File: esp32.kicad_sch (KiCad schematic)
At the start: 15 parts, among them IC3 ESP32-C3-WROOM-02-N4, J5 UART, J6 ToSSR, Q1 BSS138, SW1 SW_Push

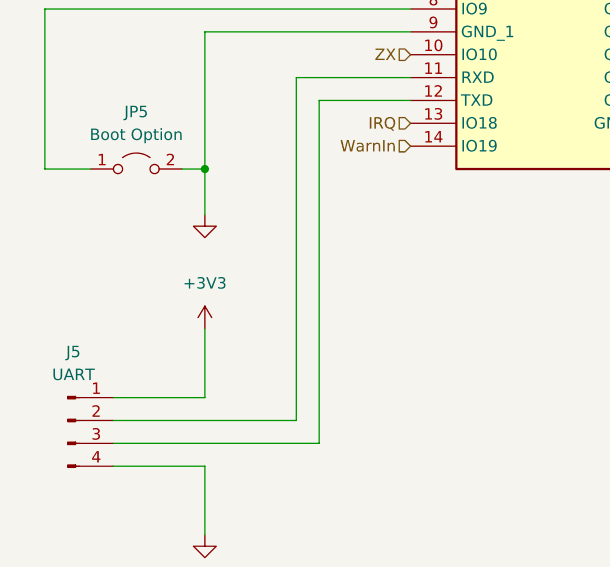
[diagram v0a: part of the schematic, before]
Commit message: feat: add +5V power symbol for uart programming
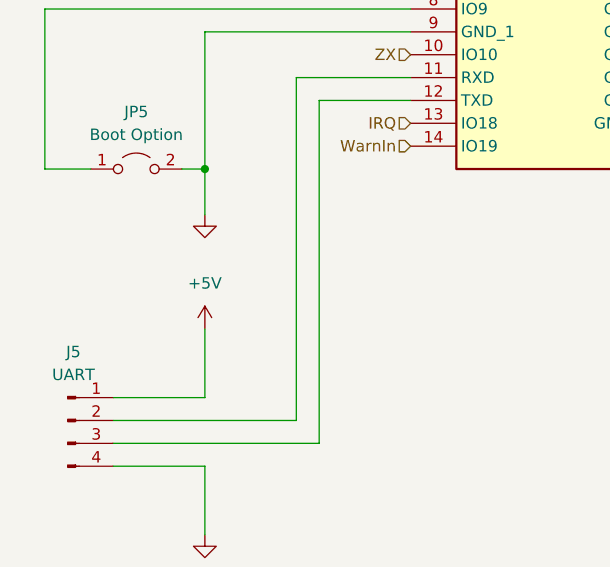
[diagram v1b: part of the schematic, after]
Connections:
- net +3V3: no longer J5.1 (Pin_1)
- new net +5V: J5.1 (Pin_1)

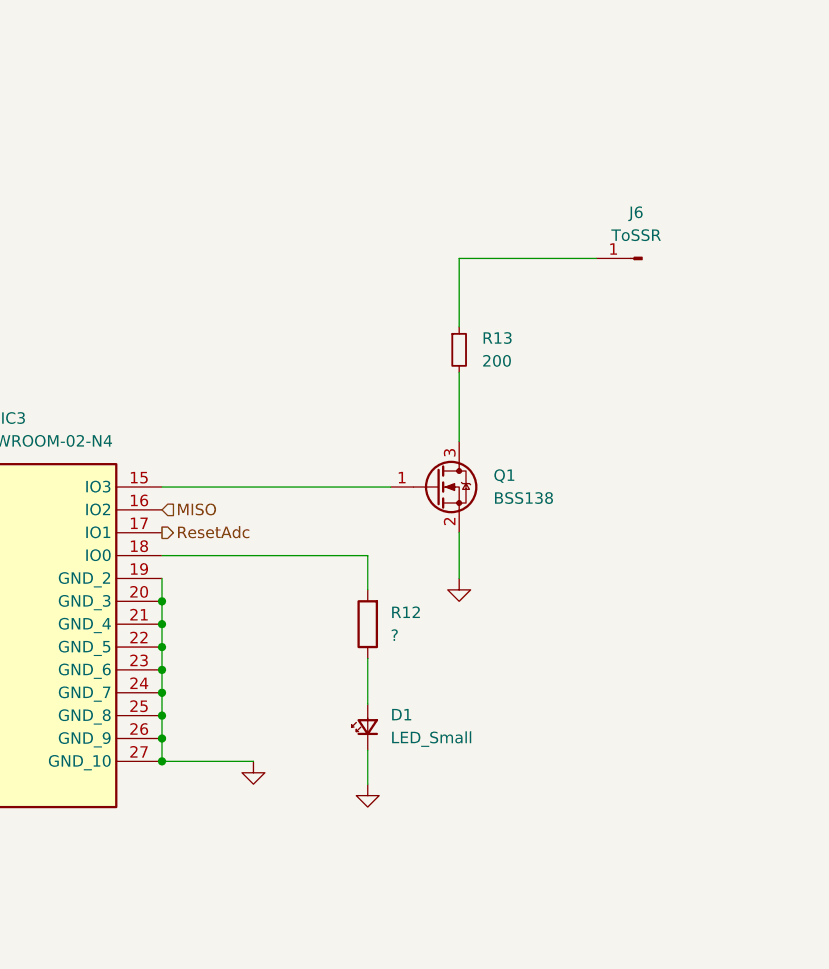
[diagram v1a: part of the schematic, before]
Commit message: fix: update esp32 strapping pad 2 to high level
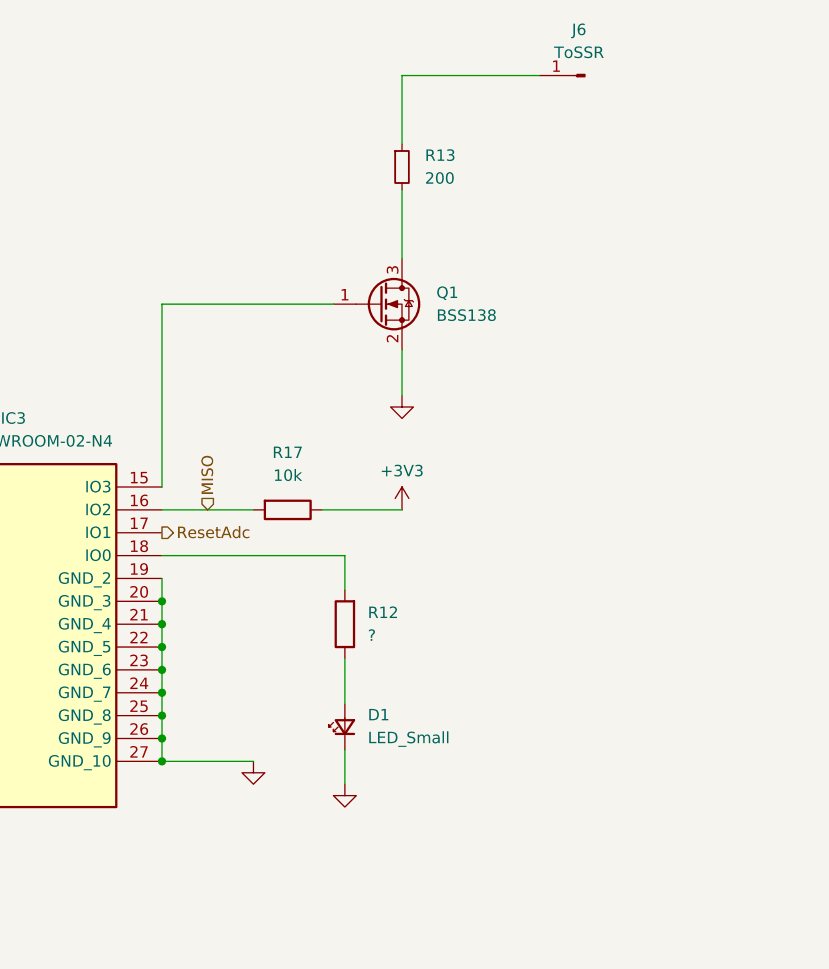
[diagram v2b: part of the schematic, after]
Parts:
- added R17: 10k, Resistor_THT:R_Axial_DIN0207_L6.3mm_D2.5mm_P7.62mm_Horizontal, symbol Device:R
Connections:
- net +3V3: now also R17.1
- net MISO: now also R17.2
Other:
- moved on the sheet: D1, J6, Q1, R12, R13

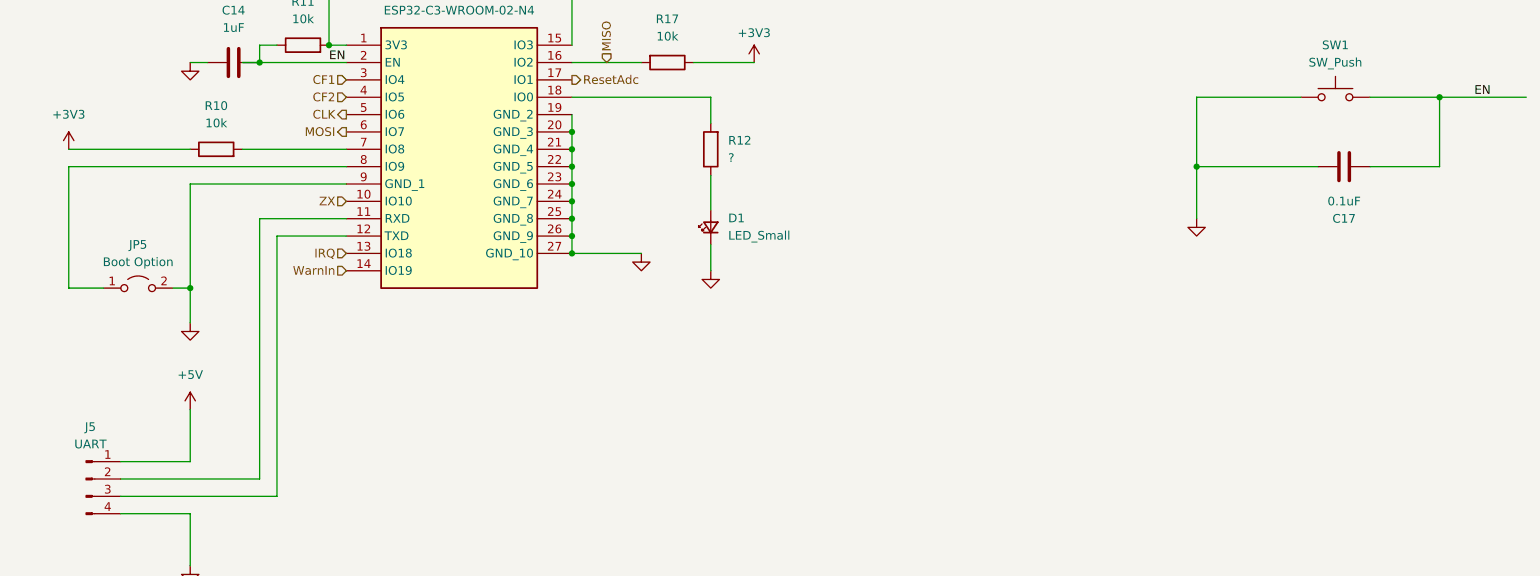
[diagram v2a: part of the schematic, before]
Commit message: fix: add boot button for esp32
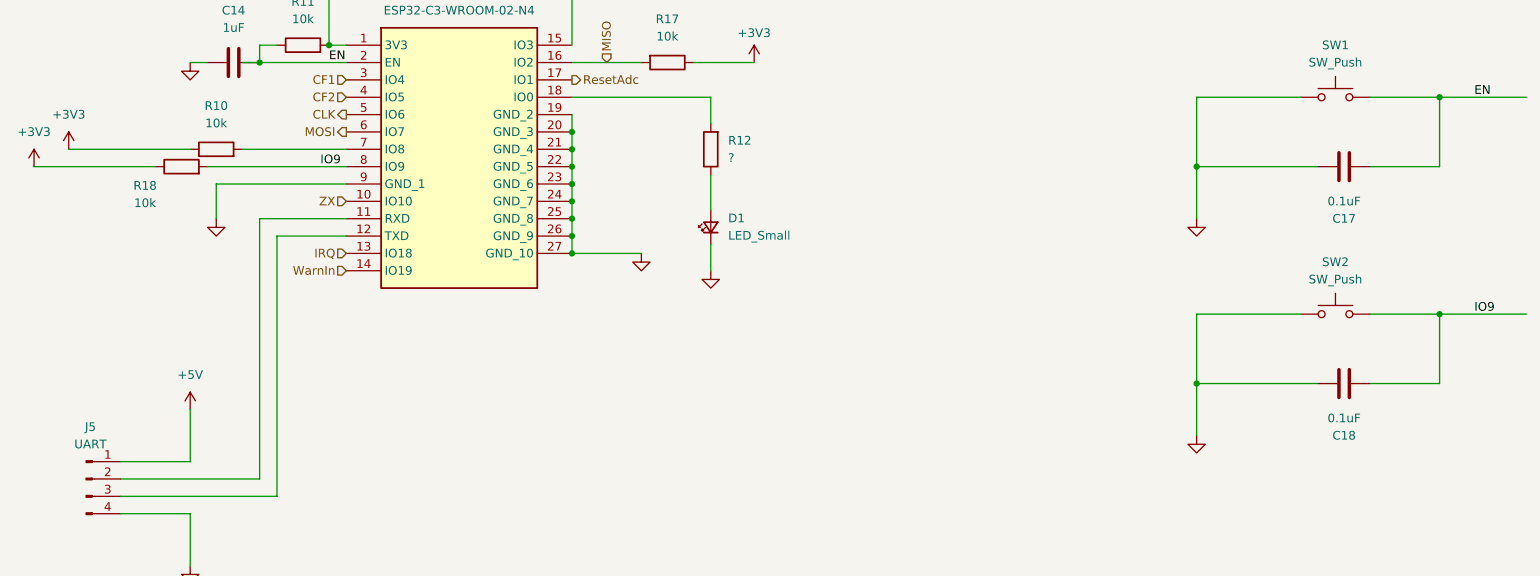
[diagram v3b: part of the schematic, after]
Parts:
- removed JP5: Boot Option, TestPoint:TestPoint_2Pads_Pitch2.54mm_Drill0.8mm, symbol Jumper:Jumper_2_Open
- added C18: 0.1uF, Capacitor_SMD:C_0805_2012Metric_Pad1.18x1.45mm_HandSolder, symbol Device:C
- added R18: 10k, Resistor_THT:R_Axial_DIN0207_L6.3mm_D2.5mm_P7.62mm_Horizontal, symbol Device:R
- added SW2: SW_Push, Button_Switch_SMD:SW_SPST_EVQQ2, symbol Switch:SW_Push
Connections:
- net +3V3: now also R18.1
- net GND: now also C18.1, SW2.1
- net IO9: now reaches IC3.8 (IO9)
- net IO9: now also C18.2, R18.2, SW2.2

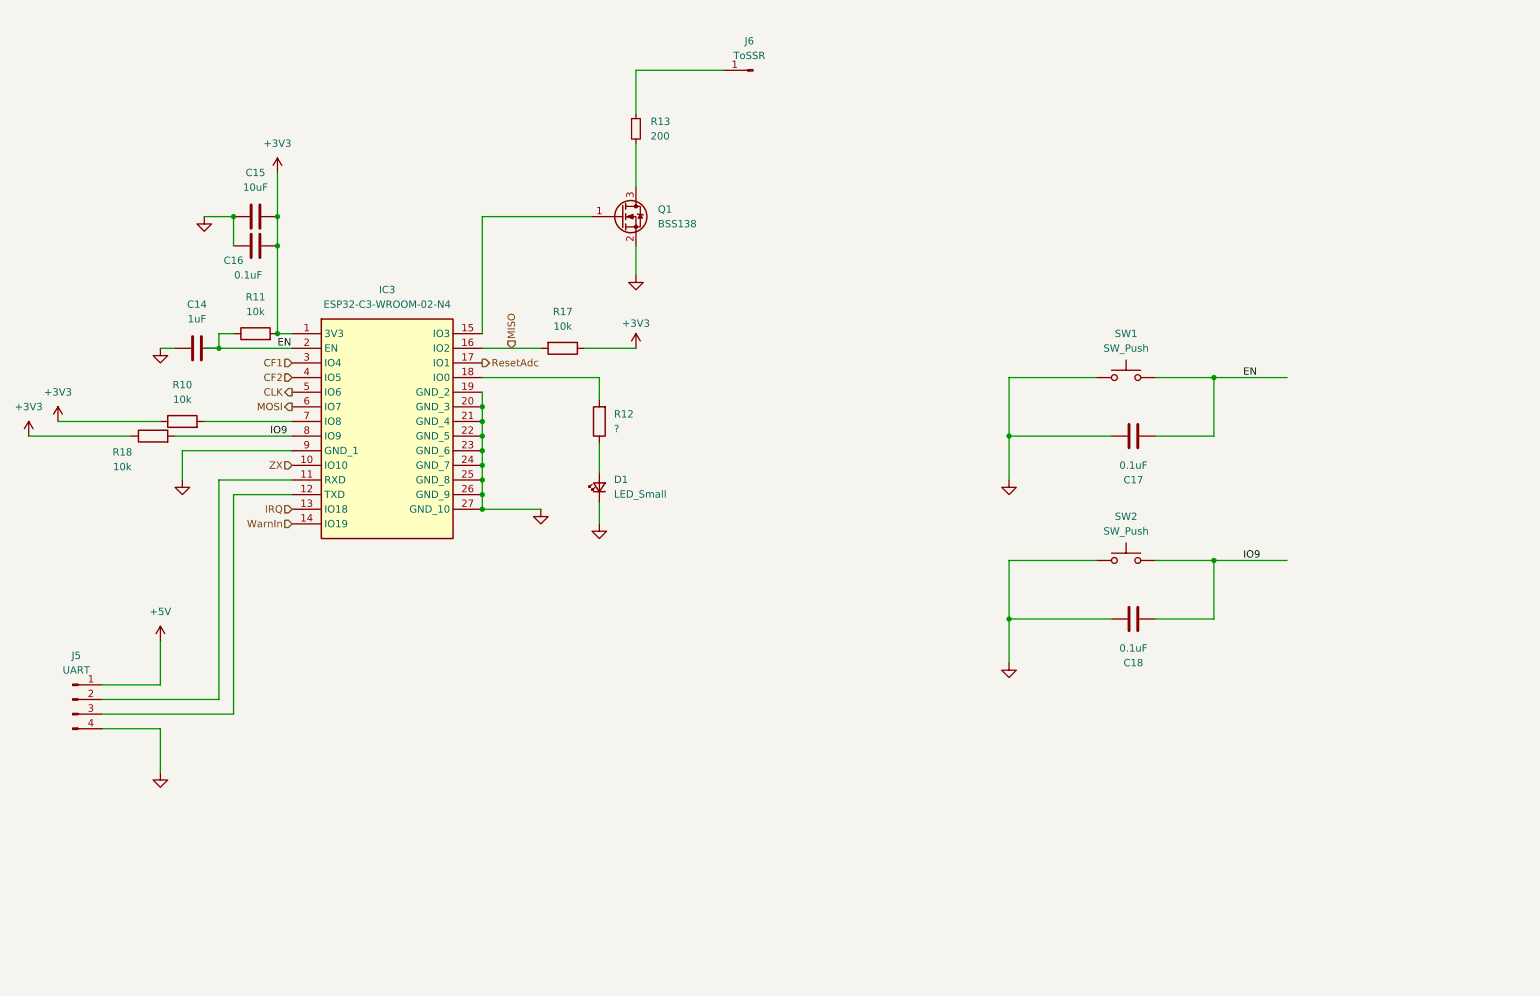
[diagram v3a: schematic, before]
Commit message: feat: substitute esp32-c3 with esp32-s3
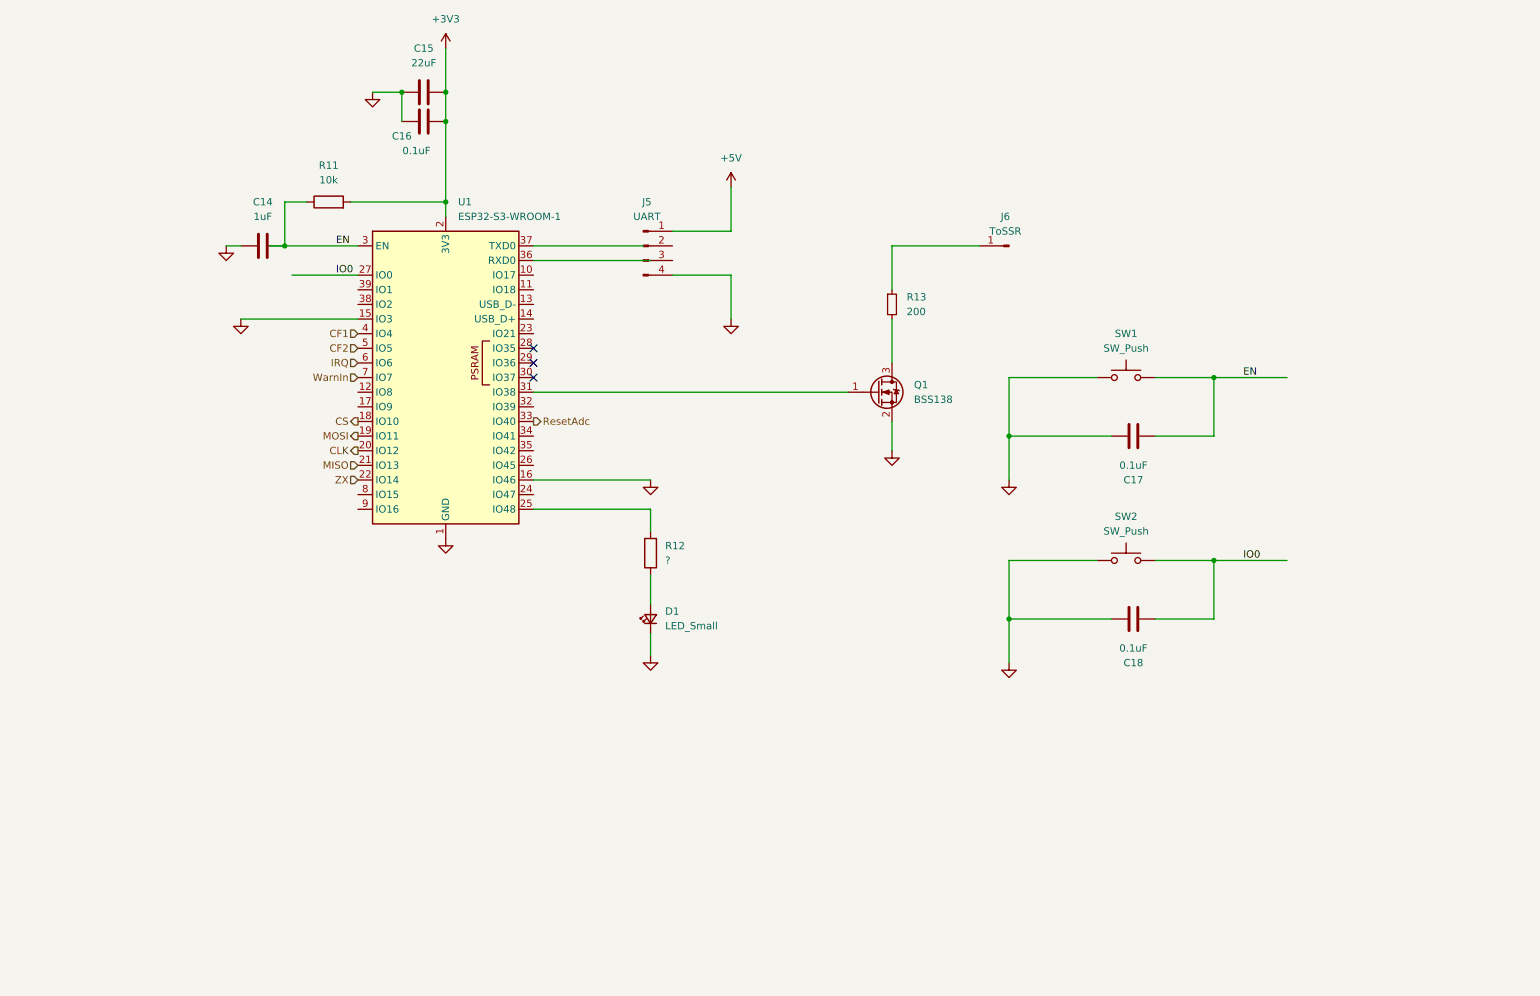
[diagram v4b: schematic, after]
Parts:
- removed IC3: ESP32-C3-WROOM-02-N4, ESP32-C3-WROOM-02-N4:ESP32C3WROOM02N4, symbol ESP32-C3-WROOM-02-N4:ESP32-C3-WROOM-02-N4
- removed R10, R17, R18: 10k, Resistor_THT:R_Axial_DIN0207_L6.3mm_D2.5mm_P7.62mm_Horizontal, symbol Device:R
- added U1: ESP32-S3-WROOM-1, RF_Module:ESP32-S3-WROOM-1, symbol RF_Module:ESP32-S3-WROOM-1
- C15: value 10uF -> 22uF
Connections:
- net +3V3: now also U1.2 (3V3)
- net CF1: now also U1.4 (IO4)
- net CF2: now also U1.5 (IO5)
- net CLK: now also U1.20 (IO12)
- net EN: now also U1.3 (EN)
- net GND: now also U1.1 (GND), U1.15 (IO3), U1.16 (IO46), U1.40 (GND), U1.41 (GND)
- net IRQ: now also U1.6 (IO6)
- net MISO: now also U1.21 (IO13)
- net MOSI: now also U1.19 (IO11)
- net ResetAdc: now also U1.33 (IO40)
- net WarnIn: now also U1.7 (IO7)
- net ZX: now also U1.22 (IO14)
- net at Q1.1 (G): now also U1.31 (IO38)
- net at R12.2: now also U1.25 (IO48)
- net IO9 renamed IO0
- net IO0: now also U1.27 (IO0)
- new net CS: U1.18 (IO10)
- no-connect marks 0 -> 3
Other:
- moved on the sheet: C14, C15, C16, D1, J5, J6, Q1, R11, R12, R13

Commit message: feat: add USB connector to ESP
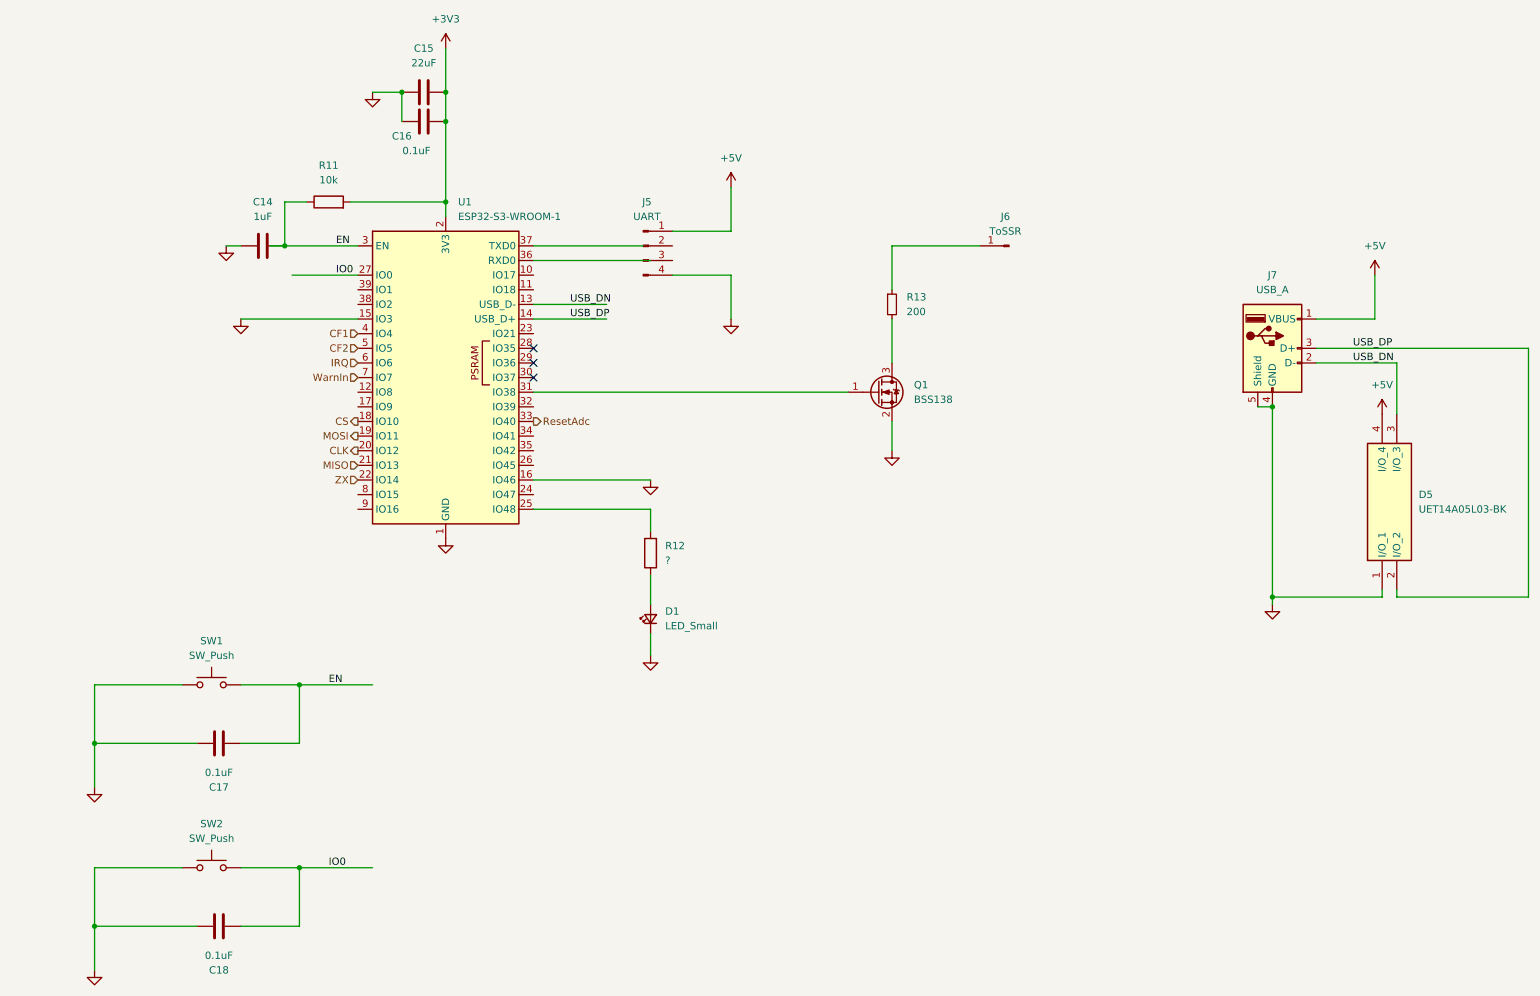
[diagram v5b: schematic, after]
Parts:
- added D5: UET14A05L03-BK, UET14A05L03BK, symbol UET14A05L03-BK:UET14A05L03-BK
- added J7: USB_A, symbol Connector:USB_A
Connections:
- net +5V: now also D5.4 (I/O_4), J7.1 (VBUS)
- net GND: now also D5.1 (I/O_1), J7.4 (GND), J7.5 (Shield)
- net USB_DN: now reaches U1.13 (USB_D-)
- net USB_DN: now also D5.3 (I/O_3), J7.2 (D-)
- net USB_DP: now reaches U1.14 (USB_D+)
- net USB_DP: now also D5.2 (I/O_2), J7.3 (D+)
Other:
- moved on the sheet: C17, C18, SW1, SW2
